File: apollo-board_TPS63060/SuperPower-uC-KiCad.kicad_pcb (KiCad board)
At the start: 4 copper layers, 45.1 x 45.1 mm, 112 parts, among them J1 JST_PH_S2B_thru, J10 Conn_01x13_Male, J11 Conn_01x04_Male, J3 Conn_01x02_Male, J4 DNP/JST_ZH_S2B_thru, J5 DNP/JST_XH_S2B_thru, J6 Conn_01x02_Male, Q1 DMN2019UTS, Q10 2N7002A, Q11 2N7002A, Q12 DMP2035UVT, Q13 DMP2035UVT, Q14 DMP2035UVT, Q15 DMN3023L, Q2 Si3421DV, Q3 DMN3023L, Q4 2N7002A, Q5 DMP2035UVT, Q6 BSS84-7-F, Q9 2N7002A, SW1 DNP/SKRKAEE020, U1 AP9101CK6-AYTRG1, U10 TPS63070RNMT, U2 USB-C, U3 IP4220CZ6, U4 LTC4162EUFD-LAD, U5 RV-3028-C7, U8 TPS70933DRVT, U9 TPS63060

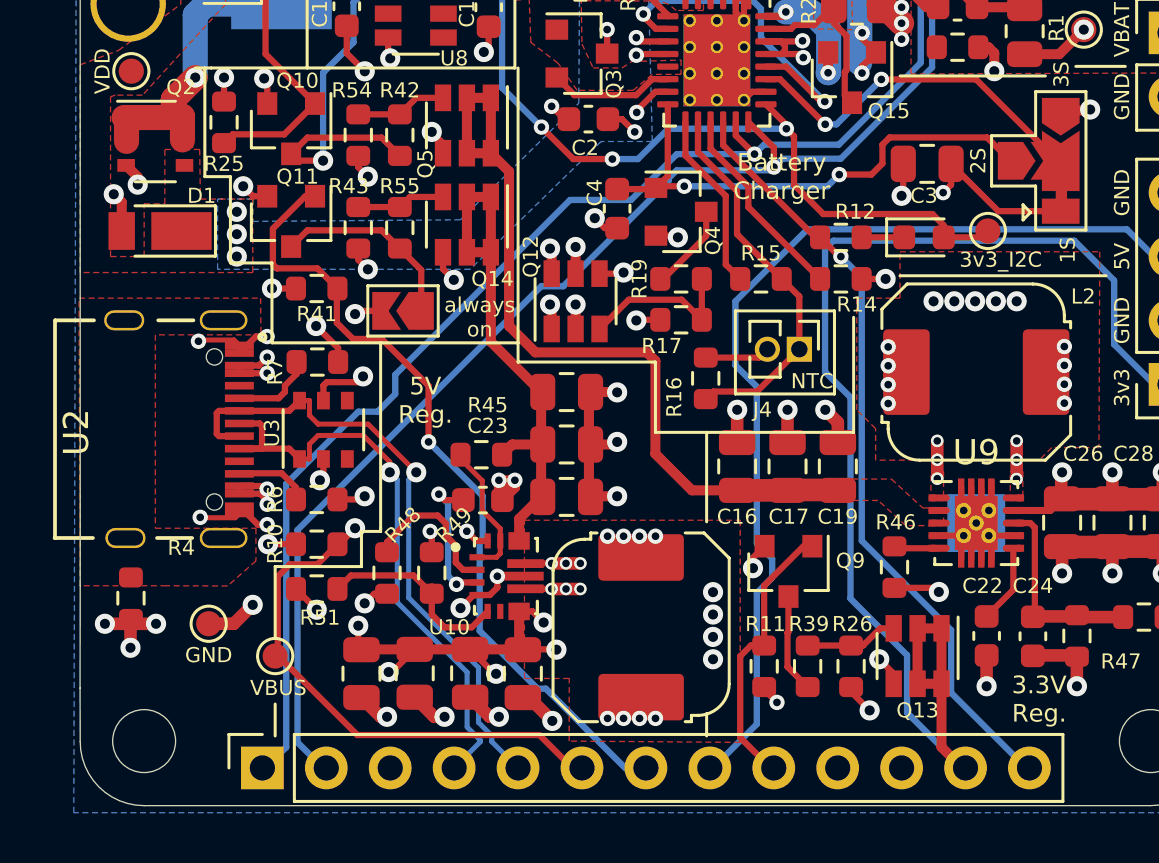
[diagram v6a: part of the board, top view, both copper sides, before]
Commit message: Place and route the 2nd TPS63060 (+5V)
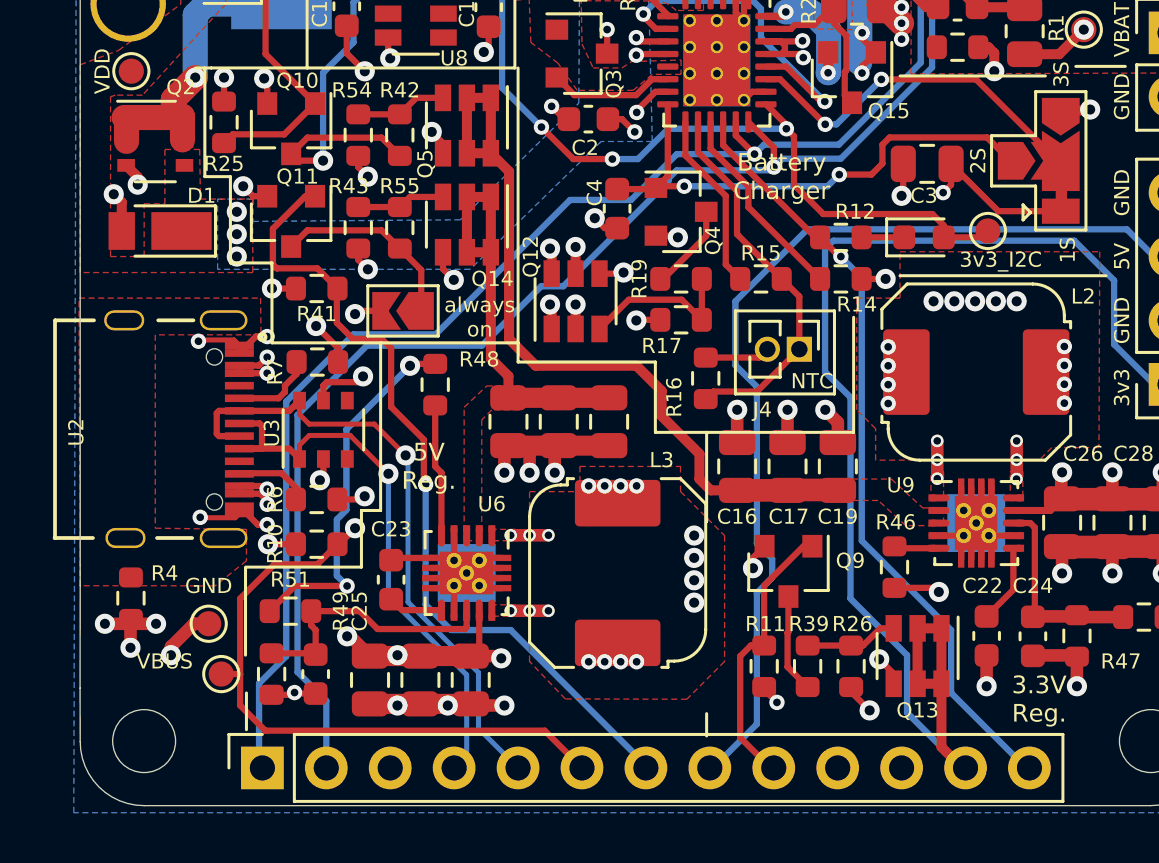
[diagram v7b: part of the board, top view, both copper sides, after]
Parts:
- removed R45: 10k, Resistor_SMD:R_0603_1608Metric
- removed U10: TPS63070RNMT, TPS63070RNM:VREG_TPS63070RNMR
- added U6: TPS63060, TPS63060:Texas_S-PWSON-N10_ThermalVias, F.Cu at (133.3, 111.0)
- C25: value 10μF -> 10pF; footprint Capacitor_SMD:C_0805_2012Metric -> Capacitor_SMD:C_0603_1608Metric
- R48: value 100k -> 1M
- moved C25 8.23 mm to (127.3, 115.0)
- moved R48 7.72 mm to (132.1, 103.5), turned to 90 degrees
- moved R49 7.53 mm to (125.6, 115.0), turned to 90 degrees
- moved C23 4.83 mm to (130.3, 111.3), turned to 90 degrees
- moved C21 3.78 mm to (135.0, 105.0), turned to 270 degrees
- moved L3 2.35 mm to (139.3, 111.0), turned to 270 degrees
- moved TP4 2.26 mm to (123.6, 115.0)
- moved C20 2.06 mm to (139.0, 105.0), turned to 270 degrees
- moved R51 1.37 mm to (126.3, 112.5)
- moved C18 0.96 mm to (137.0, 105.0), turned to 270 degrees
- moved C31 0.42 mm to (129.5, 115.2)
- moved C29 0.35 mm to (131.5, 115.2)
- moved C27 0.27 mm to (133.5, 115.2)
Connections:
- net Net-(C18-Pad1) renamed /Regulator and Cut-Off Module/5v0_Reg_Vin
- C23 pad 1: Net-(C23-Pad1) -> /Regulator and Cut-Off Module/5v0_Reg_Vaux
- C25 pad 1: /5V -> /Regulator and Cut-Off Module/5v0_Reg_FB
- R49 pad 2: Net-(R49-Pad2) -> /Regulator and Cut-Off Module/5v0_Reg_FB
- R51 pad 1: Net-(R49-Pad2) -> /Regulator and Cut-Off Module/5v0_Reg_FB
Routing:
- net /Regulator and Cut-Off Module/5v0_Reg_FB: track 0.00 -> 10.7 mm
- net Net-(R49-Pad2): track 8.09 -> 0.00 mm
- net GND: track 103.8 -> 109.8 mm, vias 80 -> 74
- net /5V: track 55.7 -> 61.7 mm, vias 7 -> 5
- net Net-(C23-Pad1): track 5.79 -> 0.00 mm, vias 2 -> 0
- net Net-(L3-Pad1): track 7.19 -> 1.50 mm
- net Net-(R45-Pad1): track 5.57 -> 0.00 mm
- net VBUS: track 32.0 -> 36.6 mm
- net /Regulator and Cut-Off Module/5v0_Reg_Vin: track 20.7 -> 16.4 mm
- net /SDA: track 69.9 -> 72.7 mm
- net /Regulator and Cut-Off Module/5v0_Reg_Vaux: track 0.00 -> 2.18 mm
- net /SCL: track 71.4 -> 73.0 mm
- net Net-(R48-Pad1): track 5.98 -> 5.00 mm
- net Net-(L3-Pad2): track 2.36 -> 1.50 mm
- net /D+: track 24.5 -> 23.7 mm
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- added copper zone on F.Cu, net /Regulator and Cut-Off Module/5v0_Reg_Vin
- added copper zone on F.Cu, net Net-(L3-Pad1)
- added copper zone on F.Cu, net Net-(L3-Pad2)

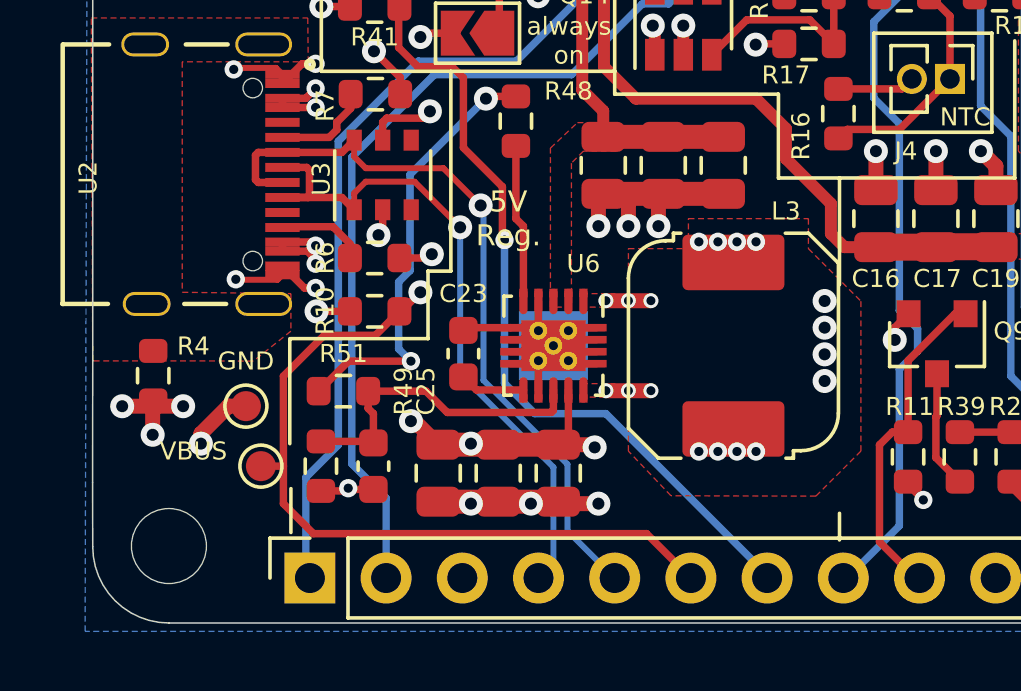
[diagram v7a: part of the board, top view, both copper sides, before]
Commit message: Update 22µF 0805 and 10pF 0603 capacitors
+ Silk Ref. Des.
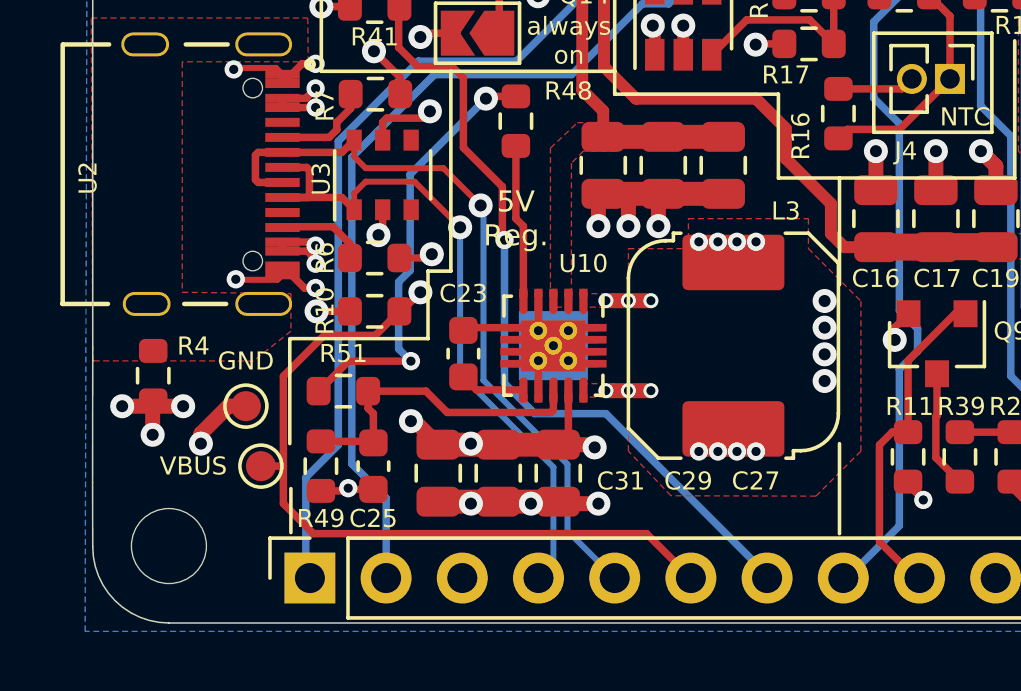
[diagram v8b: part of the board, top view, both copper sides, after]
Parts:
- C25: value 10pF -> CC0603JRNPO9BN100
- C27, C29, C31: value 22μF -> CL21A226MAQNNNE
- renumbered U6 to U10
